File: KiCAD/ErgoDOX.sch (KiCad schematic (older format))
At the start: 195 parts, among them J1 USB, J2 3.5mm, J3 JMP, J4 JMP, J5 JMP, J6 JMP, J7 USB, J8 Conn_01x05, SW1 SWITCH_PUSH, SW10 SWITCH_PUSH, SW11 SWITCH_PUSH, SW12 SWITCH_PUSH, SW13 SWITCH_PUSH, SW14 SWITCH_PUSH, SW15 SWITCH_PUSH, SW16 SWITCH_PUSH, SW17 SWITCH_PUSH, SW18 SWITCH_PUSH, SW19 SWITCH_PUSH, SW2 SWITCH_PUSH, SW20 SWITCH_PUSH, SW21 SWITCH_PUSH, SW22 SWITCH_PUSH, SW23 SWITCH_PUSH, SW24 SWITCH_PUSH, SW25 SWITCH_PUSH, SW26 SWITCH_PUSH, SW27 SWITCH_PUSH, SW28 SWITCH_PUSH, SW29 SWITCH_PUSH, SW3 SWITCH_PUSH, SW30 SWITCH_PUSH, SW31 SWITCH_PUSH, SW32 SWITCH_PUSH, SW33 SWITCH_PUSH, SW34 SWITCH_PUSH, SW35 SWITCH_PUSH, SW36 SWITCH_PUSH, SW37 SWITCH_PUSH, SW38 SWITCH_PUSH, SW39 SWITCH_PUSH, SW4 SWITCH_PUSH, SW40 SWITCH_PUSH, SW41 SWITCH_PUSH, SW42 SWITCH_PUSH, SW43 SWITCH_PUSH, SW44 SWITCH_PUSH, SW45 SWITCH_PUSH, SW46 SWITCH_PUSH, SW5 SWITCH_PUSH, SW6 SWITCH_PUSH, SW7 SWITCH_PUSH, SW8 SWITCH_PUSH, SW9 SWITCH_PUSH, U1 ProMicro

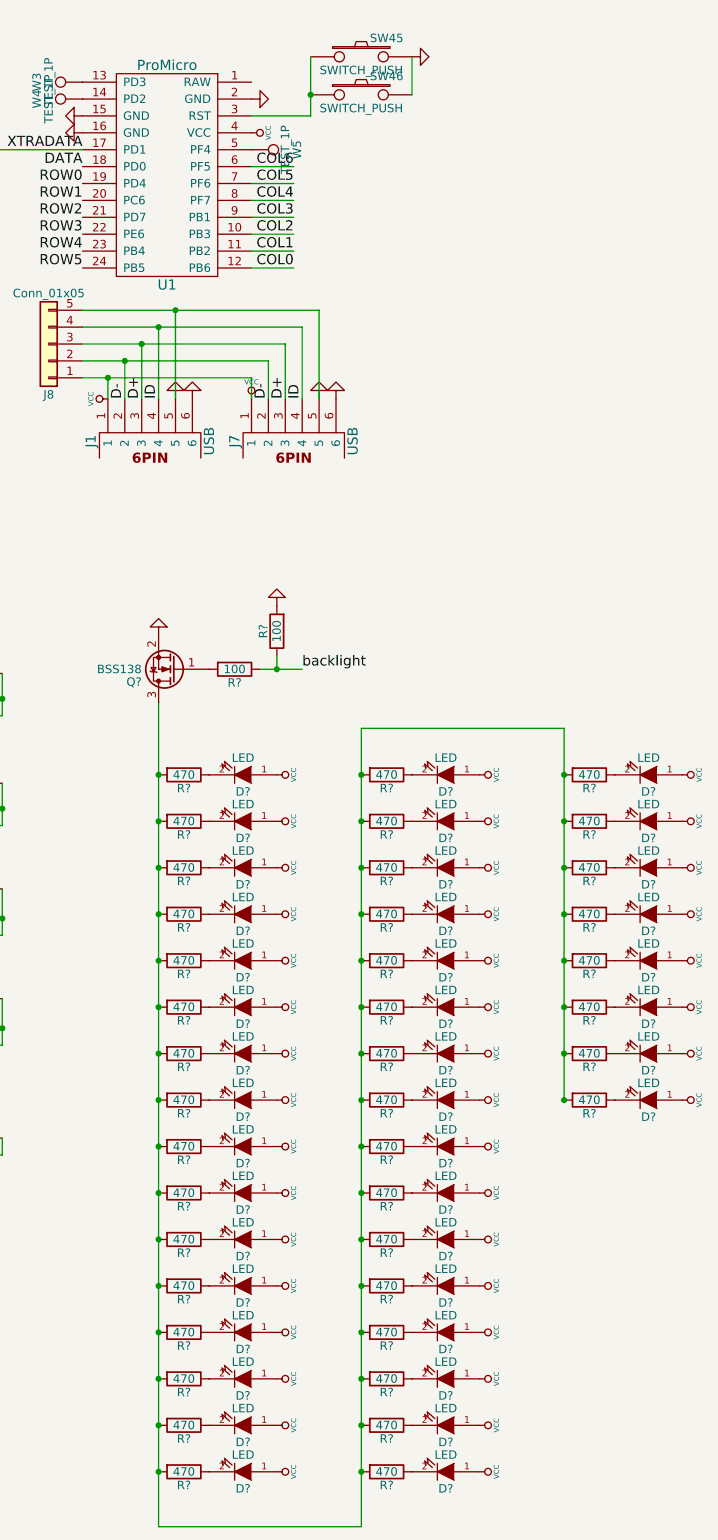
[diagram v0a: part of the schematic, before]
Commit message: led circuit and placement
finisehd placing led components and traces
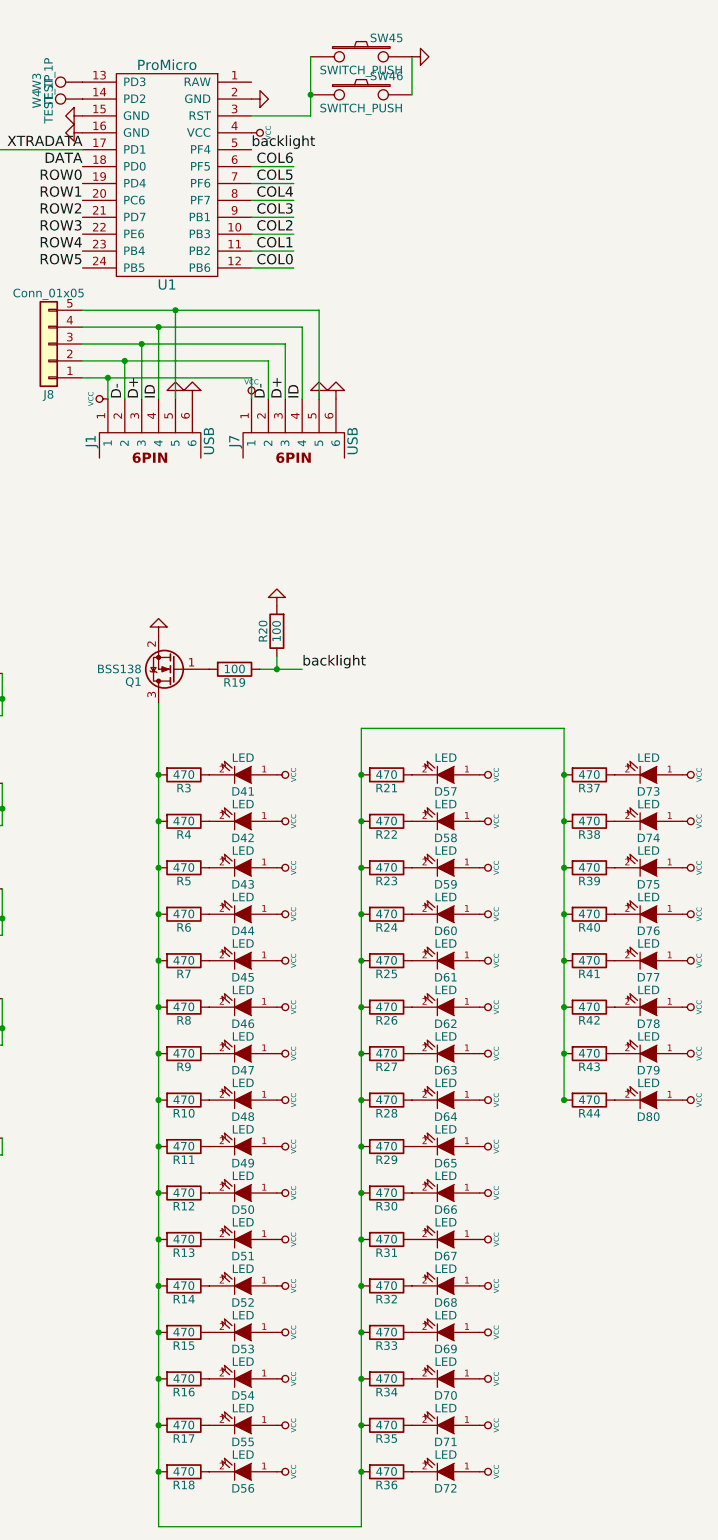
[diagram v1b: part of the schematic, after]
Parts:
- removed W5: TEST_1P, BishopKicadConsolidated:PIN_1, symbol TEST_1P
- D41, D42, D43, D44, D45, D46, D47, D48, D49, D50, D51, D52, D53, D54, D55, D56, D57, D58, D59, D60, D61, D62, D63, D64, D65, D66, D67, D68, D69, D70, D71, D72, D73, D74, D75, D76, D77, D78, D79, D80: renamed from D?; footprint (none) -> BishopKicadConsolidated:CHERRY_MX_LED
- R10, R11, R12, R13, R14, R15, R16, R17, R18, R19, R20, R21, R22, R23, R24, R25, R26, R27, R28, R29, R3, R30, R31, R32, R33, R34, R35, R36, R37, R38, R39, R4, R40, R41, R42, R43, R44, R5, R6, R7, R8, R9: renamed from R?; footprint (none) -> SMD_Packages:SMD-1206_Pol
- gave numbers to parts that had none: 1
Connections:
- net backlight: now also U1.5 (PF4)
